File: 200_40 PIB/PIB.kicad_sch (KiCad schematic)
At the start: 52 parts, among them J1 M80-5100442, J11 53261-0271, J13 53261-0271, J15 53261-0571, J17 53261-0271, J18 53261-0271, J3 G125-MS12605M2P, Q11 IRF7832, Q9 IRF7832, U4 STM32G431RBTx, U5 ADM1270ACPZ, Y1 ECS-80-18-4XDN

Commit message: pib work
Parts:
- removed J17, J18: 53261-0271, Connector_Molex:Molex_PicoBlade_53261-0271_1x02-1MP_P1.25mm_Horizontal, symbol Connector:Conn_01x02_Pin
- added C21, C28: 1uF, Capacitor_SMD:C_0603_1608Metric, symbol Device:C
- added C29, C30: 10nF, Capacitor_SMD:C_0603_1608Metric, symbol Device:C
- added J2: 53261-0471, Connector_Molex:Molex_PicoBlade_53261-0471_1x04-1MP_P1.25mm_Horizontal, symbol Connector:Conn_01x04_Pin
- added Q1: Si7489DP, Package_SO:PowerPAK_SO-8_Single, symbol Transistor_FET:Si7141DP
- added R35: 15m, Resistor_SMD:R_0402_1005Metric, symbol Device:R
- added R36, R37: 4.7K, Resistor_SMD:R_0402_1005Metric, symbol Device:R
- added R48: 2K, Resistor_SMD:R_0201_0603Metric, symbol Device:R
- added R49, R54: 1K, Resistor_SMD:R_0603_1608Metric, symbol Device:R
- added R50: 33K, Capacitor_SMD:C_0603_1608Metric, symbol Device:R
- added R51: 0R, Resistor_SMD:R_0402_1005Metric, symbol Device:R
- added R52: 10K, Resistor_SMD:R_0402_1005Metric, symbol Device:R
- added R53: 100K, Resistor_SMD:R_0402_1005Metric, symbol Device:R
- added R55: 10K, Resistor_SMD:R_0603_1608Metric, symbol Device:R
- C9: value 1uF 16V X7R -> 4.7uF
- R13, R14: value 4.7k -> 4.7K
- R4: value 22k -> 22K
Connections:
- net SCL is gone; now on net INT_I2C_SCL: R14.1, R16.1
- net SDA is gone; now on net INT_I2C_SDA: R13.1, R15.1
- net +3.3V: now also R36.2, R37.2
- net BAT_HOT: now also U5.15 (VCC), C28.1, J2.2 (Pin_2), J2.3 (Pin_3), R35.2, R50.2
- net DISCHARGE_EN: now also R52.1
- net EXT_I2C_SCL: now also R36.1
- net EXT_I2C_SDA: now also R37.1
- net GND: now also U5.17 (EP), U5.7 (GND), C21.2, C28.2, C29.2, C30.2, R48.1, R53.1, R54.1
- net at Q9.5 (D), Q9.6 (D), Q9.7 (D)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: now also J2.4 (Pin_4)
- net at Q11.5 (D), Q11.6 (D), Q11.7 (D)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: now also J2.1 (Pin_1)
- net at U5.1 (VCAP): now also U5.2 (ISET), C21.1
- net at U5.10 (FB_PG): now also R54.2, R55.1
- net at U5.13 (GATE): now also Q1.4 (G)
- net at U5.14 (SENSE-): now also Q1.1 (S), Q1.2 (S), Q1.3 (S), R35.1
- net at U5.3 (UV): now also R49.2, R50.1
- net at U5.4 (OV): now also R48.2, R49.1
- net at U5.5 (ENABLE): now also R51.1, R52.2, R53.2
- net at U5.6 (~{FAULT}): now also R51.2
- net at U5.8 (TIMER): now also C30.1
- net at U5.9 (TIMER_OFF): now also C29.1
- new net VBAT_DCHG: Q1.5 (D), R55.2
- no-connect marks 3 -> 4
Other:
- note added: "12V UVLO, 18V OVLO"
- note added: "3.33A OCP"
- moved on the sheet: C5, C9, Q11, R13, R14, R15, R16, R34, R9

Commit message: work
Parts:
- added C32, C33: 1uF, Capacitor_SMD:C_0603_1608Metric, symbol Device:C
- added C34, C35: 10nF, Capacitor_SMD:C_0603_1608Metric, symbol Device:C
- added C36: 100nF, Capacitor_SMD:C_0402_1005Metric, symbol Device:C
- added Q2: Si7489DP, Package_SO:PowerPAK_SO-8_Single, symbol Transistor_FET:Si7141DP
- added R56, R67, R68: 10K, Resistor_SMD:R_0603_1608Metric, symbol Device:R
- added R57, R66: 33K, Resistor_SMD:R_0603_1608Metric, symbol Device:R
- added R58, R62, R70: 10K, Resistor_SMD:R_0402_1005Metric, symbol Device:R
- added R59: 33K, Capacitor_SMD:C_0603_1608Metric, symbol Device:R
- added R60, R69: 1K, Resistor_SMD:R_0603_1608Metric, symbol Device:R
- added R61: 2K, Resistor_SMD:R_0201_0603Metric, symbol Device:R
- added R63: 100K, Resistor_SMD:R_0402_1005Metric, symbol Device:R
- added R64: 0R, Resistor_SMD:R_0402_1005Metric, symbol Device:R
- added R65: 100m, Resistor_SMD:R_0402_1005Metric, symbol Device:R
- added R71: 10K, symbol Device:R
- added SW1: 6mm tact, Button_Switch_THT:SW_PUSH_6mm, symbol Switch:SW_Push
- added U7: ADM1270ACPZ, Package_CSP:LFCSP-16-1EP_3x3mm_P0.5mm_EP1.5x1.5mm, symbol Power_Management:ADM1270ACPZ
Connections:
- net ADC1_IN14 is gone; now on net ADC_TANK_NTC_1: U4.33 (PB11)
- net ADC1_IN15 is gone; now on net ADC_TANK_NTC_2: U4.24 (PB0)
- net +3.3V: now also R58.2, R70.2, R71.1
- net BAT_HOT: now also C33.1, R59.2, R65.2, U7.15 (VCC)
- net GND: now also C32.2, C33.2, C34.2, C35.2, R56.1, R61.1, R63.1, R67.1, R69.1, U7.17 (EP), U7.7 (GND)
- net IGNITER_EN: now also R62.1
- net VBAT_DCHG: now also R57.2
- net nRST: now also C36.1, R71.2, SW1.2
- net ADC_TANK_NTC_2: now reaches C20.1, J11.1 (Pin_1), R3.1
- net DISCHARGE_PGOOD: now reaches U4.2 (PC13)
- net DISCHARGE_PGOOD: now also U5.12 (PWRGD), R58.1
- net IGNITER_PGOOD: now reaches U4.3 (PC14)
- net IGNITER_PGOOD: now also R70.1, U7.12 (PWRGD)
- net ADC_TANK_NTC_1: now reaches C19.1, J13.1 (Pin_1), R4.1
- net at U5.11 (FLB): now also R56.2, R57.1
- net ADC1_IN1 renamed ADC_V_DCHG
- net ADC1_IN11 renamed ADC_NTC_DCHG
- net ADC1_IN12 renamed ADC_NTC_PIB
- net ADC1_IN2 renamed ADC_I_DCHG
- net ADC1_IN4 renamed ADC_V_IGN_SUPPLY
- net ADC1_IN5 renamed ADC_V_IGN_PK
- net ADC1_IN6 renamed ADC_V_IGN_INT
- net ADC1_IN7 renamed ADC_I_IGN_PK
- net ADC1_IN8 renamed ADC_Q_IGN
- net ADC1_IN9 renamed ADC_NTC_IGN
- new net: C34.1, U7.9 (TIMER_OFF)
- new net: R68.1, R69.2, U7.10 (FB_PG)
- new net: R59.1, R60.2, U7.3 (UV)
- new net: R60.1, R61.2, U7.4 (OV)
- new net: C36.2, SW1.1
- new net: Q2.1 (S), Q2.2 (S), Q2.3 (S), R65.1, U7.14 (SENSE-)
- new net: Q2.4 (G), U7.13 (GATE)
- new net: C35.1, U7.8 (TIMER)
- new net: R66.1, R67.2, U7.11 (FLB)
- new net: C32.1, U7.1 (VCAP), U7.2 (ISET)
- new net: R62.2, R63.2, R64.1, U7.5 (ENABLE)
- new net: R64.2, U7.6 (~{FAULT})
- new net VBAT_IGN: Q2.5 (D), R66.2, R68.2
- no-connect marks 4 -> 5
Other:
- sheet Valve Driver ports: added EGSE_OPEN; removed none
- note added: "500mA OCP"
- note added: "Somewhat arbitrary FLB pin setting since FLB cannot be given a voltage >6V"
- moved on the sheet: C19, C20, C5, C9, J11, J13, J15, R13, R14, R15, R16, R3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

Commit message: continue pib work
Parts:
- added C37, C38, C39, C4: 10uF, symbol Device:C
- added C40: 10nF, symbol Device:C_Small
- added C41: 10nF, Capacitor_SMD:C_0402_1005Metric, symbol Device:C
- added C42: 22pF, Capacitor_SMD:C_0402_1005Metric, symbol Device:C
- added C43: 100nF, Capacitor_SMD:C_0402_1005Metric, symbol Device:C
- added D1: D_Schottky, symbol Device:D_Schottky
- added J5: Picoblade, Connector_Molex:Molex_PicoBlade_53261-0771_1x07-1MP_P1.25mm_Horizontal, symbol Connector:Conn_01x07_Socket
- added J7: SWD, Connector_PinHeader_2.54mm:PinHeader_1x04_P2.54mm_Vertical, symbol Connector:Conn_01x04_Pin
- added L1, L2: L, symbol Device:L
- added R72, R73: 10K, Resistor_SMD:R_0402_1005Metric, symbol Device:R
- added R74: 100K, Resistor_SMD:R_0402_1005Metric, symbol Device:R
- added R75: 60.4K, Resistor_SMD:R_0402_1005Metric, symbol Device:R
- added R76, R77: 10K, symbol Device:R
- added U10: LT8580EDD, 0_PAY_Footprint_Library:DFN-8_DD, symbol 0_PAY_Symbol_Library:LT8580EDD_PBF
- added U12: MAX823TEUK_T, 0_PAY_Footprint_Library:SOT95P280X145-5N, symbol 0_PAY_Symbol_Library:MAX823TEUK_T
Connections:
- net +3.3V: now also C43.1, R77.1, U12.5 (VCC)
- net +5V: now also C39.2, L1.1, R72.2, U10.3 (VIN)
- net ADC_V_IGN_SUPPLY: now also J5.4 (Pin_4)
- net GND: now also C36.2, SW1.1, C37.1, C38.1, C39.1, C41.2, C42.2, C43.2, J5.1 (Pin_1), J7.4 (Pin_4), R74.1, R76.2, U10.8 (SYNC), U12.2 (GND)
- net IGNITER_PULSE: now also J5.7 (Pin_7)
- net SWDCLK: now also J7.3 (Pin_3)
- net SWDIO: now also J7.2 (Pin_2)
- net WDG_IN: now also R76.1, U12.4 (WDI)
- net nRST: now also J7.1 (Pin_1), R77.2, U12.1 (~{RESET}); no longer C36.1, R71.2, SW1.2
- new net: C36.1, R71.2, SW1.2, U12.3 (~{MR})
- new net: C41.1, R73.1
- new net: C42.1, R73.2, U10.2 (VC)
- new net: R75.2, U10.1 (FBX)
- new net: C4.1, L1.2, U10.4 (SW)
- new net: R72.1, U10.5 (~{SHDN})
- new net: R74.2, U10.6 (RT)
- new net: C40.1, U10.7 (SS)
- new net: C40.2, D1.1 (K), U10.9 (GND)
- new net: C4.2, D1.2 (A), L2.1
- new net -5V: C37.2, C38.2, J5.2 (Pin_2), L2.2, R75.1
- new net 5V: J5.3 (Pin_3)
- new net IgniterI: J5.6 (Pin_6)
- new net IgniterV: J5.5 (Pin_5)
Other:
- added sheet Igniter Signal Processing (Igniter Signal Processing.kicad_sch)
- note added: "-5V Supply"
- note added: "Discharge Supply Switch"
- note added: "External Connectors"
- note added: "Igniter Supply Switch"
- note added: "Valve Drive"
- note removed: "Connectors"
- moved on the sheet: C21, C26, C27, C28, C29, C30, C32, C33, C34, C35, J2, Q1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

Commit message: work
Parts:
- removed J5: Picoblade, Connector_Molex:Molex_PicoBlade_53261-0771_1x07-1MP_P1.25mm_Horizontal, symbol Connector:Conn_01x07_Socket
- removed J7: SWD, Connector_PinHeader_2.54mm:PinHeader_1x04_P2.54mm_Vertical, symbol Connector:Conn_01x04_Pin
- added C44: 100nF, Capacitor_SMD:C_0402_1005Metric, symbol Device:C
- added J5: 53261-1371, Connector_Molex:Molex_PicoBlade_53261-1371_1x13-1MP_P1.25mm_Horizontal, symbol Connector:Conn_01x13_Pin
- added J8: SWD/DEBUG, Connector_PinSocket_2.54mm:PinSocket_2x03_P2.54mm_Vertical, symbol Connector_Generic:Conn_02x03_Odd_Even
- added R78: 10K, Resistor_SMD:R_0402_1005Metric, symbol Device:R
- added R80, R81: 22, Resistor_SMD:R_0402_1005Metric, symbol Device:R
- added U14: 74LS08, symbol 74xx:74LS08
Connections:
- net ADC_Q_IGN is gone; now on net ADC_I_IGN_PK: U4.10 (PC2)
- net GNDREF is gone; now on net GND: C19.2, C20.2, J11.2 (Pin_2), J13.2 (Pin_2)
- net -5V: now also J5.8 (Pin_8)
- net 5V: now also J5.7 (Pin_7)
- net ADC_I_IGN_PK: now also J5.4 (Pin_4); no longer U4.9 (PC1)
- net ADC_NTC_IGN: now also C44.1, J5.3 (Pin_3), R78.1
- net ADC_V_IGN_PK: now also J5.5 (Pin_5)
- net ADC_V_IGN_SUPPLY: now also J5.6 (Pin_6)
- net ARM/~{SAFE}: now also U14.1, U14.4, U14.9
- net DISCHARGE_EN: now also U14.5; no longer R52.1
- net GND: now also C44.2, J5.10 (Pin_10), J5.11 (Pin_11), J5.9 (Pin_9), J8.6 (Pin_6)
- net IGNITER_EN: now also U14.2; no longer R62.1
- net IGNITER_PULSE: now also U14.10
- net IGNITER_RST: now also J5.2 (Pin_2)
- net SWDCLK: now also J8.3 (Pin_3)
- net SWDIO: now also J8.1 (Pin_1)
- net VBAT_IGN: now also J5.12 (Pin_12), J5.13 (Pin_13)
- net VDDA: now also R78.2
- net nRST: now also J8.5 (Pin_5)
- net ADC_V_IGN_INT: no longer names the net of U4.8 (PC0)
- net ADC_V_IGN_INT: now also R80.2
- new net: R81.2, U4.9 (PC1)
- new net DEBUG_UART_RX: J8.2 (Pin_2), R80.1
- new net DEBUG_UART_TX: J8.4 (Pin_4), R81.1
- new net DISCHARGE_EN_GATED: R52.1, U14.6
- new net IGNITER_EN_GATED: R62.1, U14.3
- new net IGNITER_PULSE_GATED: J5.1 (Pin_1), U14.8
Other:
- removed sheet Igniter Signal Processing
- added sheet Rogowski Integrator (Rogowski.kicad_sch)

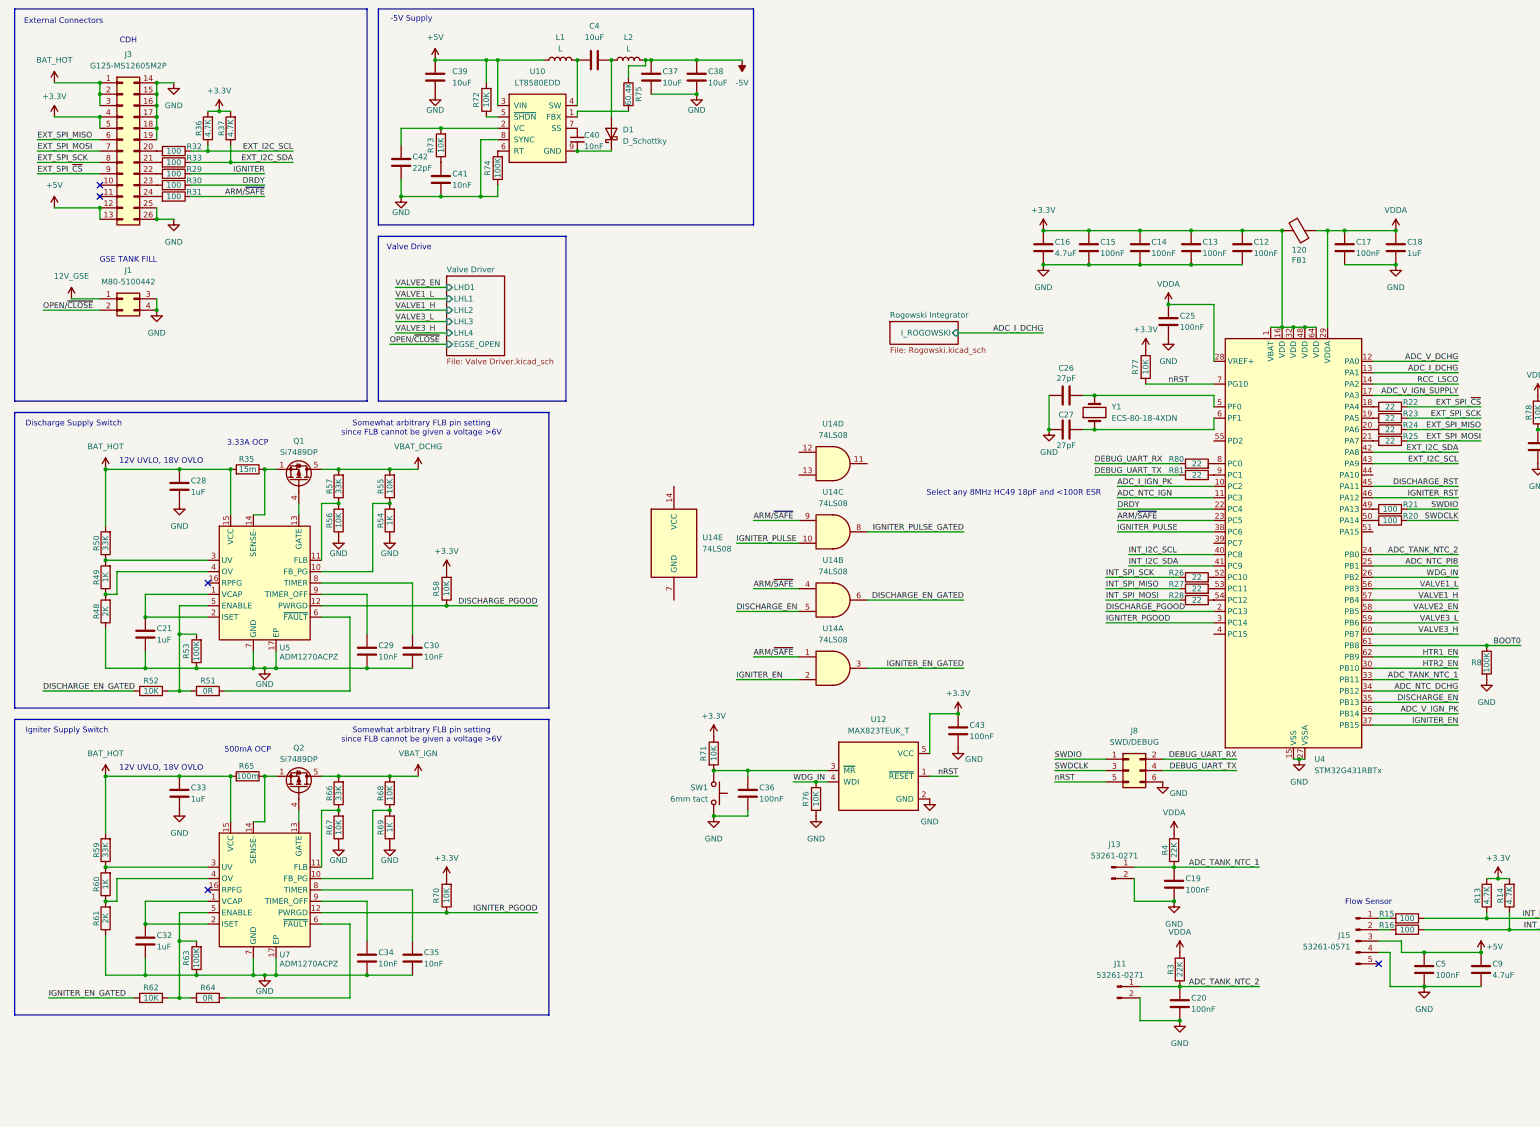
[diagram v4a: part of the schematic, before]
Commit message: assign PIB footprints, push ioc file to CubeMX 6.18.1
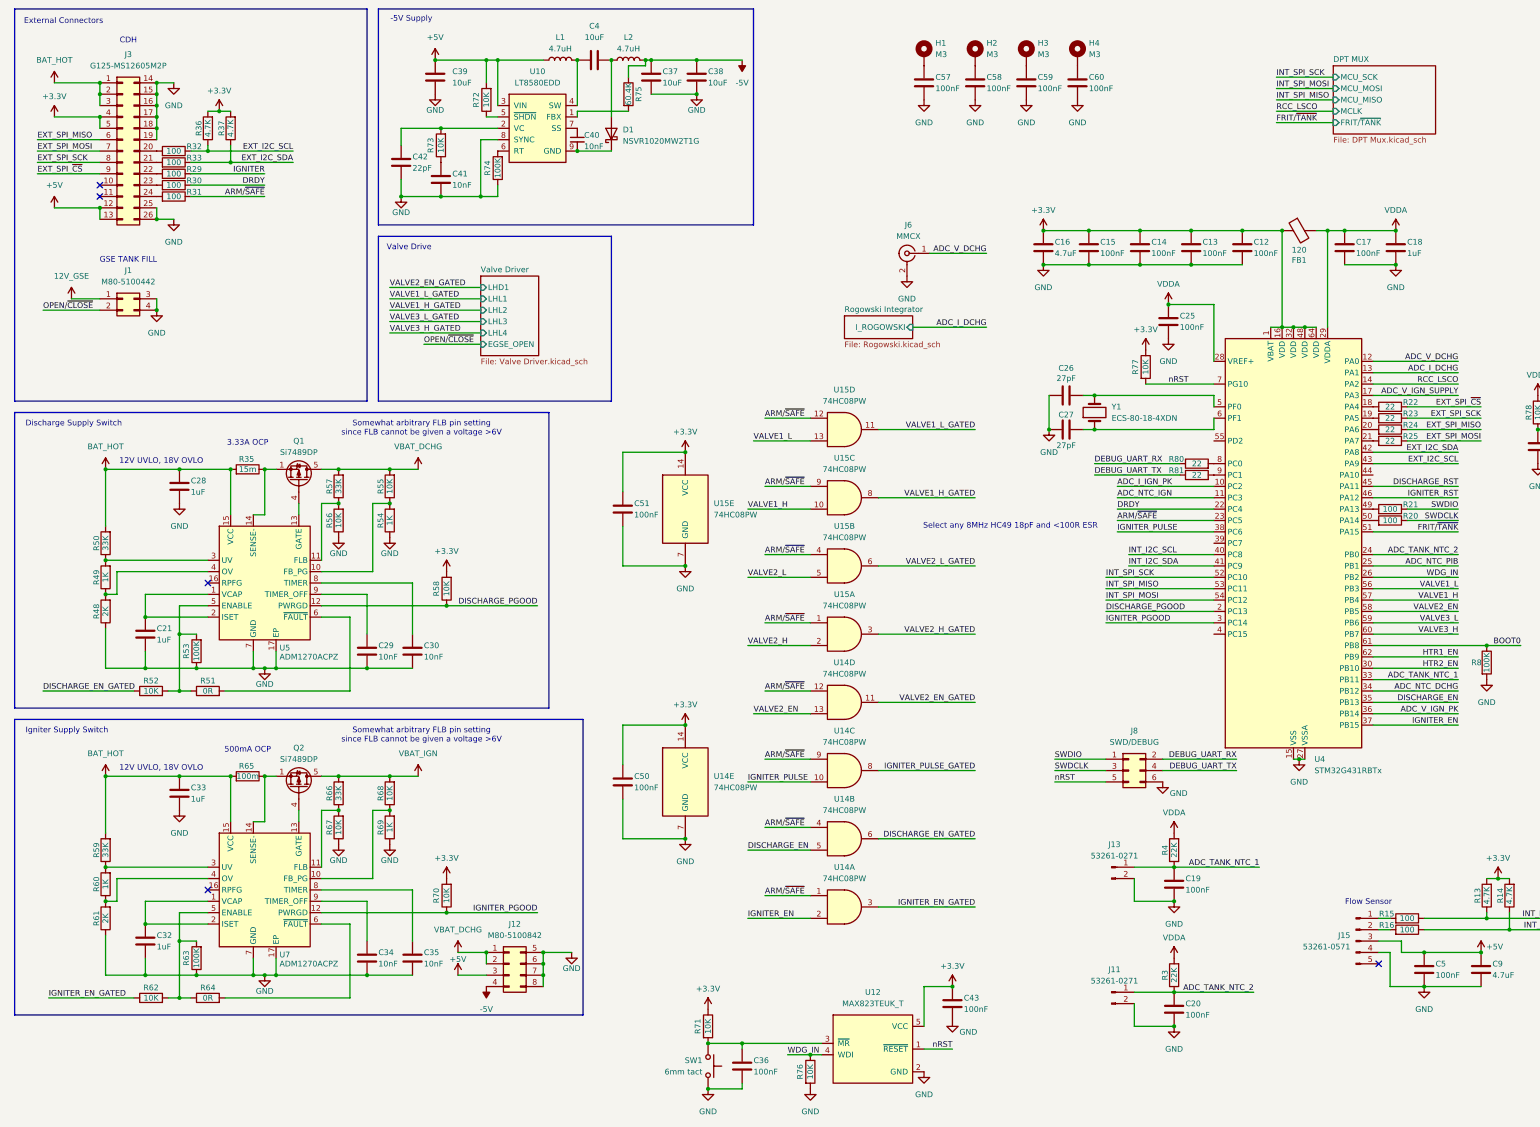
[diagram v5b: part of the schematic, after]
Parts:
- removed R26, R27, R28: 22, Resistor_SMD:R_0402_1005Metric, symbol Device:R
- added C50, C51, C57, C58, C59, C60: 100nF, Capacitor_SMD:C_0603_1608Metric, symbol Device:C
- added H1, H2, H3, H4: M3, MountingHole:MountingHole_3.2mm_M3_DIN965_Pad, symbol Mechanical:MountingHole_Pad
- added J12: M80-5100842, 0_PAY_Footprint_Library:HARWIN_M80-5100842, symbol Connector_Generic:Conn_02x04_Top_Bottom
- added J6: MMCX, Connector_Coaxial:MMCX_Molex_73415-0961_Horizontal_1.6mm-PCB, symbol Connector:Conn_Coaxial
- added U15: 74HC08PW, Package_SO:TSSOP-14_4.4x5mm_P0.65mm, symbol 74xx:74LS08
- C36, C41, C42, C43, C44, C5: footprint Capacitor_SMD:C_0402_1005Metric -> Capacitor_SMD:C_0603_1608Metric
- C37, C38, C39, C4: footprint (none) -> Capacitor_SMD:C_0805_2012Metric
- C40: footprint (none) -> Capacitor_SMD:C_0603_1608Metric
- D1: value D_Schottky -> NSVR1020MW2T1G; footprint (none) -> Diode_SMD:D_SOD-323
- FB1: footprint Package_LCC:PLCC-84_29.3x29.3mm_P1.27mm -> Resistor_SMD:R_0603_1608Metric
- J1: footprint Package_LCC:PLCC-84_29.3x29.3mm_P1.27mm -> 0_PAY_Footprint_Library:HARWIN_M80-5100442
- L1, L2: value L -> 4.7uH; footprint (none) -> Inductor_SMD:L_Vishay_IHLP-1616
- R13, R14, R15, R16, R19, R20, R21, R3, R34, R36, R37, R4, R51, R52, R53, R58, R62, R63, R64, R65, R70, R72, R73, R74, R75, R78: footprint Resistor_SMD:R_0402_1005Metric -> Resistor_SMD:R_0603_1608Metric
- R35: footprint Resistor_SMD:R_0402_1005Metric -> Resistor_SMD:R_0805_2012Metric
- R48, R61: footprint Resistor_SMD:R_0201_0603Metric -> Resistor_SMD:R_0603_1608Metric
- R50, R59: footprint Capacitor_SMD:C_0603_1608Metric -> Resistor_SMD:R_0603_1608Metric
- R7, R71, R76, R77, R8, R9: footprint (none) -> Resistor_SMD:R_0603_1608Metric
- U14: value 74LS08 -> 74HC08PW; footprint (none) -> Package_SO:TSSOP-14_4.4x5mm_P0.65mm
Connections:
- net +3.3V: now also U14.14 (VCC), C50.1, C51.1, U15.14 (VCC)
- net +5V: now also J12.3 (Pin_3)
- net -5V: now also J12.4 (Pin_4)
- net ADC_V_DCHG: now also J6.1 (In)
- net ARM/~{SAFE}: now also U14.12, U15.1, U15.12, U15.4, U15.9
- net GND: now also U14.7 (GND), C50.2, C51.2, C57.2, C58.2, C59.2, C60.2, J12.5 (Pin_5), J12.6 (Pin_6), J12.7 (Pin_7), J12.8 (Pin_8), J6.2 (Ext), U15.7 (GND)
- net INT_SPI_MISO: now also U4.53 (PC11)
- net INT_SPI_MOSI: now also U4.54 (PC12)
- net INT_SPI_SCK: now also U4.52 (PC10)
- net VALVE1_H: now also U15.10
- net VALVE1_L: now also U15.13
- net VALVE2_EN: now also U14.13
- net VBAT_DCHG: now also J12.1 (Pin_1), J12.2 (Pin_2)
- net VALVE2_EN_GATED: now reaches U14.11
- net FRIT/~{TANK}: now reaches U4.51 (PA15)
- new net: C58.1, H2.1
- new net: C57.1, H1.1
- new net: C60.1, H4.1
- new net: C59.1, H3.1
- new net VALVE1_H_GATED: U15.8
- new net VALVE1_L_GATED: U15.11
- new net VALVE2_H: U15.2
- new net VALVE2_H_GATED: U15.3
- new net VALVE2_L: U15.5
- new net VALVE2_L_GATED: U15.6
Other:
- added sheet DPT MUX (DPT Mux.kicad_sch)
- moved on the sheet: C20, C36, C43, J11, R3, R71, R76, SW1, U12, U14A, U14B, U14C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
